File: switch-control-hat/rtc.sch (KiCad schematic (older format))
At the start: 3 parts, among them U2 DS3231M

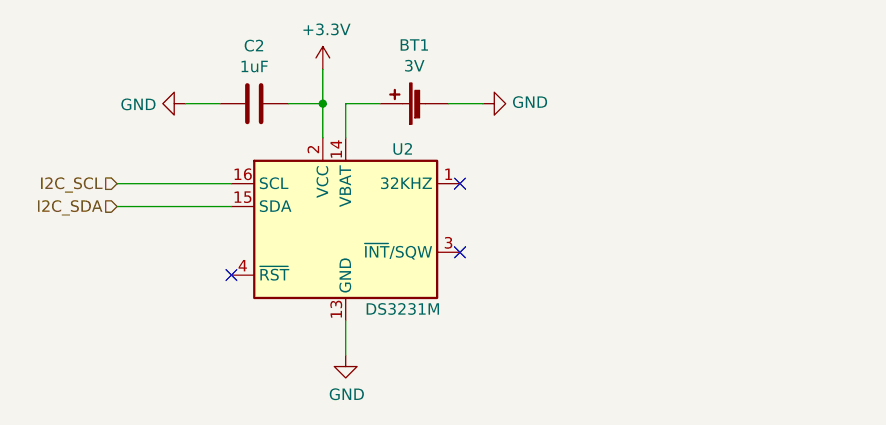
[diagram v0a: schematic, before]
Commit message: Fixed ERC and DRC errors
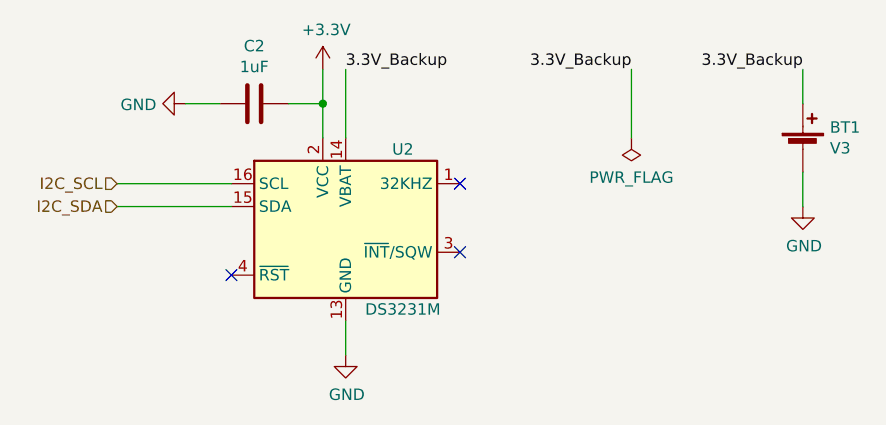
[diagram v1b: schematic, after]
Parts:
- BT1: value 3V -> V3
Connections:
- net 3.3V_Backup: now reaches BT1.1 (+), U2.14 (VBAT)
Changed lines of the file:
@@
 Sheet 4 6
 Title ""
-Date ""
+Date "2020-03-06"
 Rev ""
 Comp ""
@@
 Comment4 ""
 $EndDescr
-Wire Wire Line
-	6200 3500 6350 3500
-$Comp
-L power:GND #PWR?
-U 1 1 5E62F0E0
-P 6350 3500
-AR Path="/5E62F0E0" Ref="#PWR?"  Part="1"
-AR Path="/5E624F1D/5E62F0E0" Ref="#PWR0138"  Part="1"
-F 0 "#PWR0138" H 6350 3250 50  0001 C CNN
-F 1 "GND" V 6355 3372 50  0000 R CNN
-F 2 "" H 6350 3500 50  0001 C CNN
-F 3 "" H 6350 3500 50  0001 C CNN
-	1    6350 3500
-	0    -1   -1   0
-$EndComp
-Wire Wire Line
-	5750 3500 5900 3500
-Wire Wire Line
-	5750 3650 5750 3500
-$Comp
-L Device:Battery_Cell BT?
-U 1 1 5E62F0E8
-P 6100 3500
-AR Path="/5E62F0E8" Ref="BT?"  Part="1"
-AR Path="/5E624F1D/5E62F0E8" Ref="BT1"  Part="1"
-F 0 "BT1" V 6355 3550 50  0000 C CNN
-F 1 "3V" V 6264 3550 50  0000 C CNN
-F 2 "Battery:BatteryHolder_Keystone_3000_1x12mm" V 6100 3560 50  0001 C CNN
-F 3 "~" V 6100 3560 50  0001 C CNN
-	1    6100 3500
-	0    -1   -1   0
-$EndComp
 Connection ~ 5650 3500
 Wire Wire Line
@@
 Wire Wire Line
 	5750 4450 5750 4600
+$Comp
+L Device:Battery_Cell BT1
+U 1 1 5E674E0B
+P 7750 3700
+F 0 "BT1" H 7868 3796 50  0000 L CNN
+F 1 "V3" H 7868 3705 50  0000 L CNN
+F 2 "Battery:BatteryHolder_Keystone_3000_1x12mm" V 7750 3760 50  0001 C CNN
+F 3 "~" V 7750 3760 50  0001 C CNN
+	1    7750 3700
+	1    0    0    -1
+$EndComp
+Text Label 7750 3350 2    50   ~ 0
+3.3V_Backup
+$Comp
+L power:GND #PWR0138
+U 1 1 5E6762AD
+P 7750 3950
+F 0 "#PWR0138" H 7750 3700 50  0001 C CNN
+F 1 "GND" H 7755 3777 50  0000 C CNN
+F 2 "" H 7750 3950 50  0001 C CNN
+F 3 "" H 7750 3950 50  0001 C CNN
+	1    7750 3950
+	1    0    0    -1
+$EndComp
+Wire Wire Line
+	7750 3350 7750 3500
+Wire Wire Line
+	7750 3800 7750 3950
+Text Label 7000 3350 2    50   ~ 0
+3.3V_Backup
+$Comp
+L power:PWR_FLAG #FLG0105
+U 1 1 5E6795B4
+P 7000 3650
+F 0 "#FLG0105" H 7000 3725 50  0001 C CNN
+F 1 "PWR_FLAG" H 7000 3823 50  0000 C CNN
+F 2 "" H 7000 3650 50  0001 C CNN
+F 3 "~" H 7000 3650 50  0001 C CNN
+	1    7000 3650
+	-1   0    0    1
+$EndComp
+Wire Wire Line
+	7000 3650 7000 3350
+Text Label 5750 3350 0    50   ~ 0
+3.3V_Backup
+Wire Wire Line
+	5750 3350 5750 3650
 $EndSCHEMATC
